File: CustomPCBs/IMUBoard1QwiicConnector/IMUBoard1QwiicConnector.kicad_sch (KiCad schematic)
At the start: 14 parts, among them J1 Conn_01x04_Pin, Y1 32.768kHz

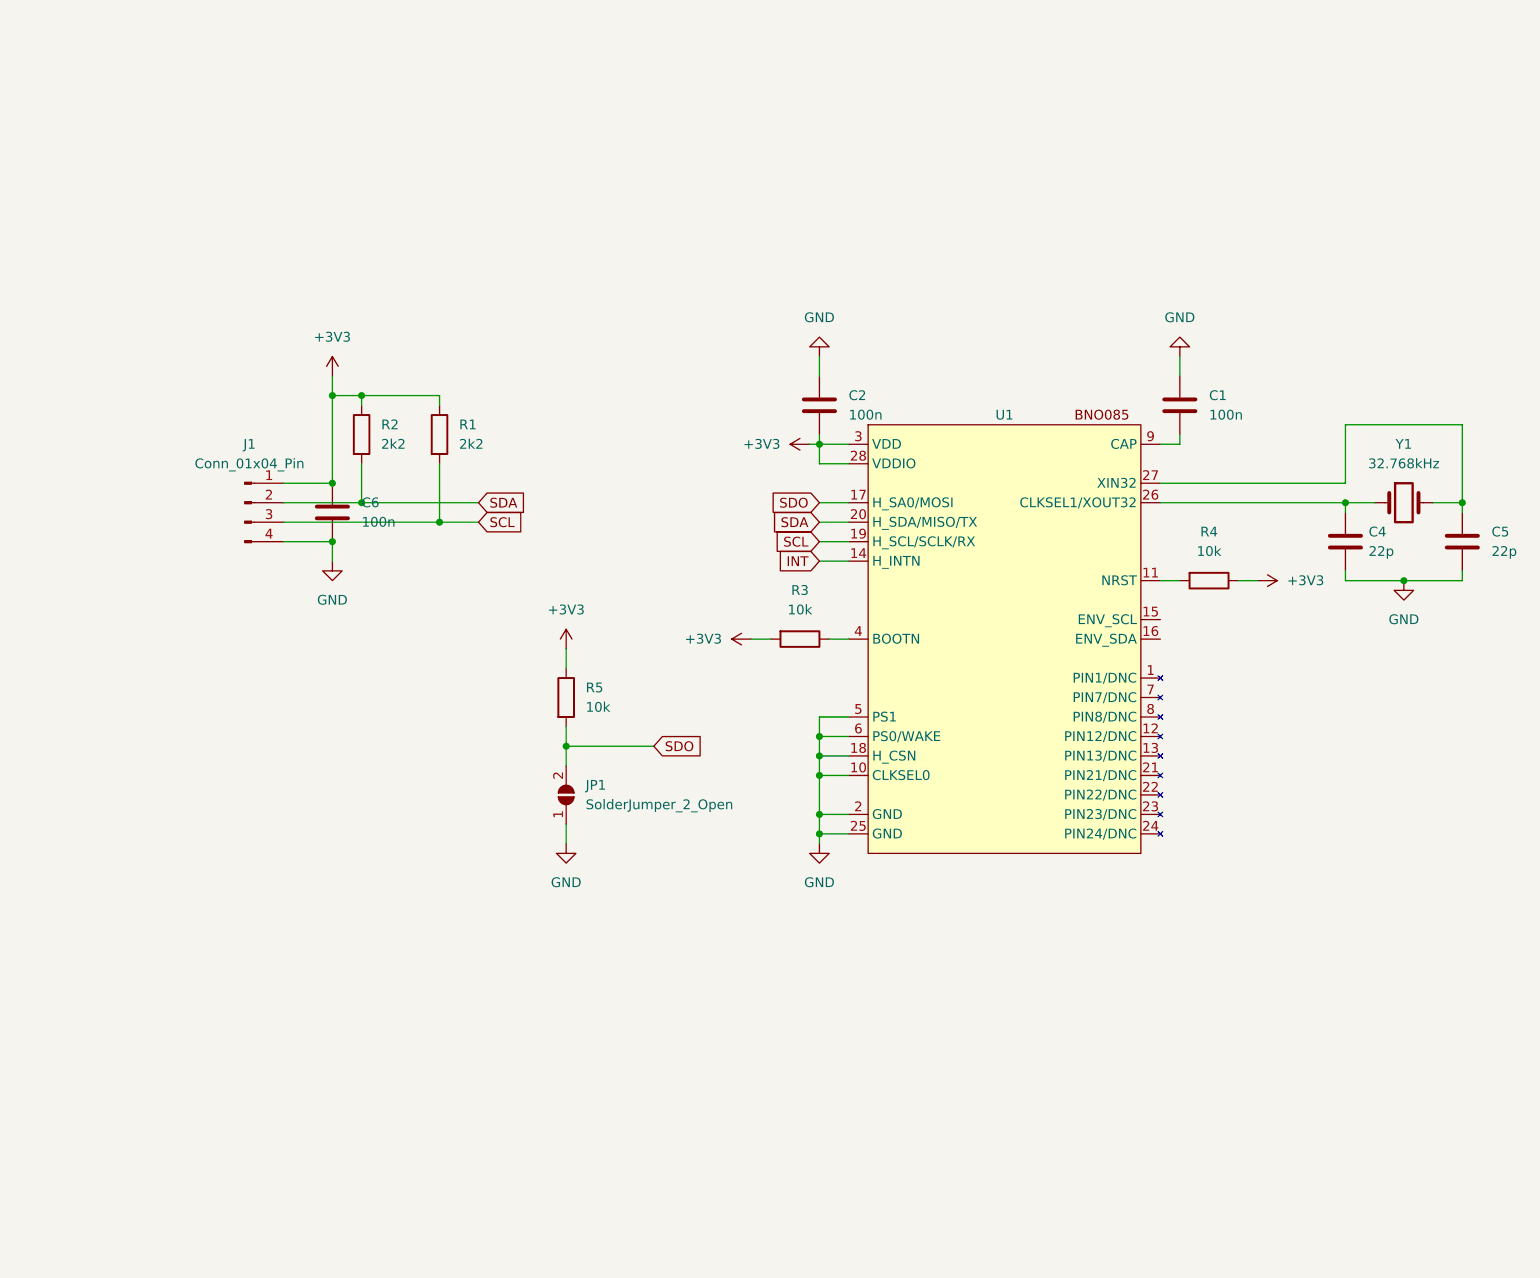
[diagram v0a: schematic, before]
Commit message: Updating smallest IMU board
Will probably make it even smaller by hardwiring PS0, PS1 and SDO pins.
And maybe even the connector can go to give room for a cable bundle of 4
wires soldered to the board directly.
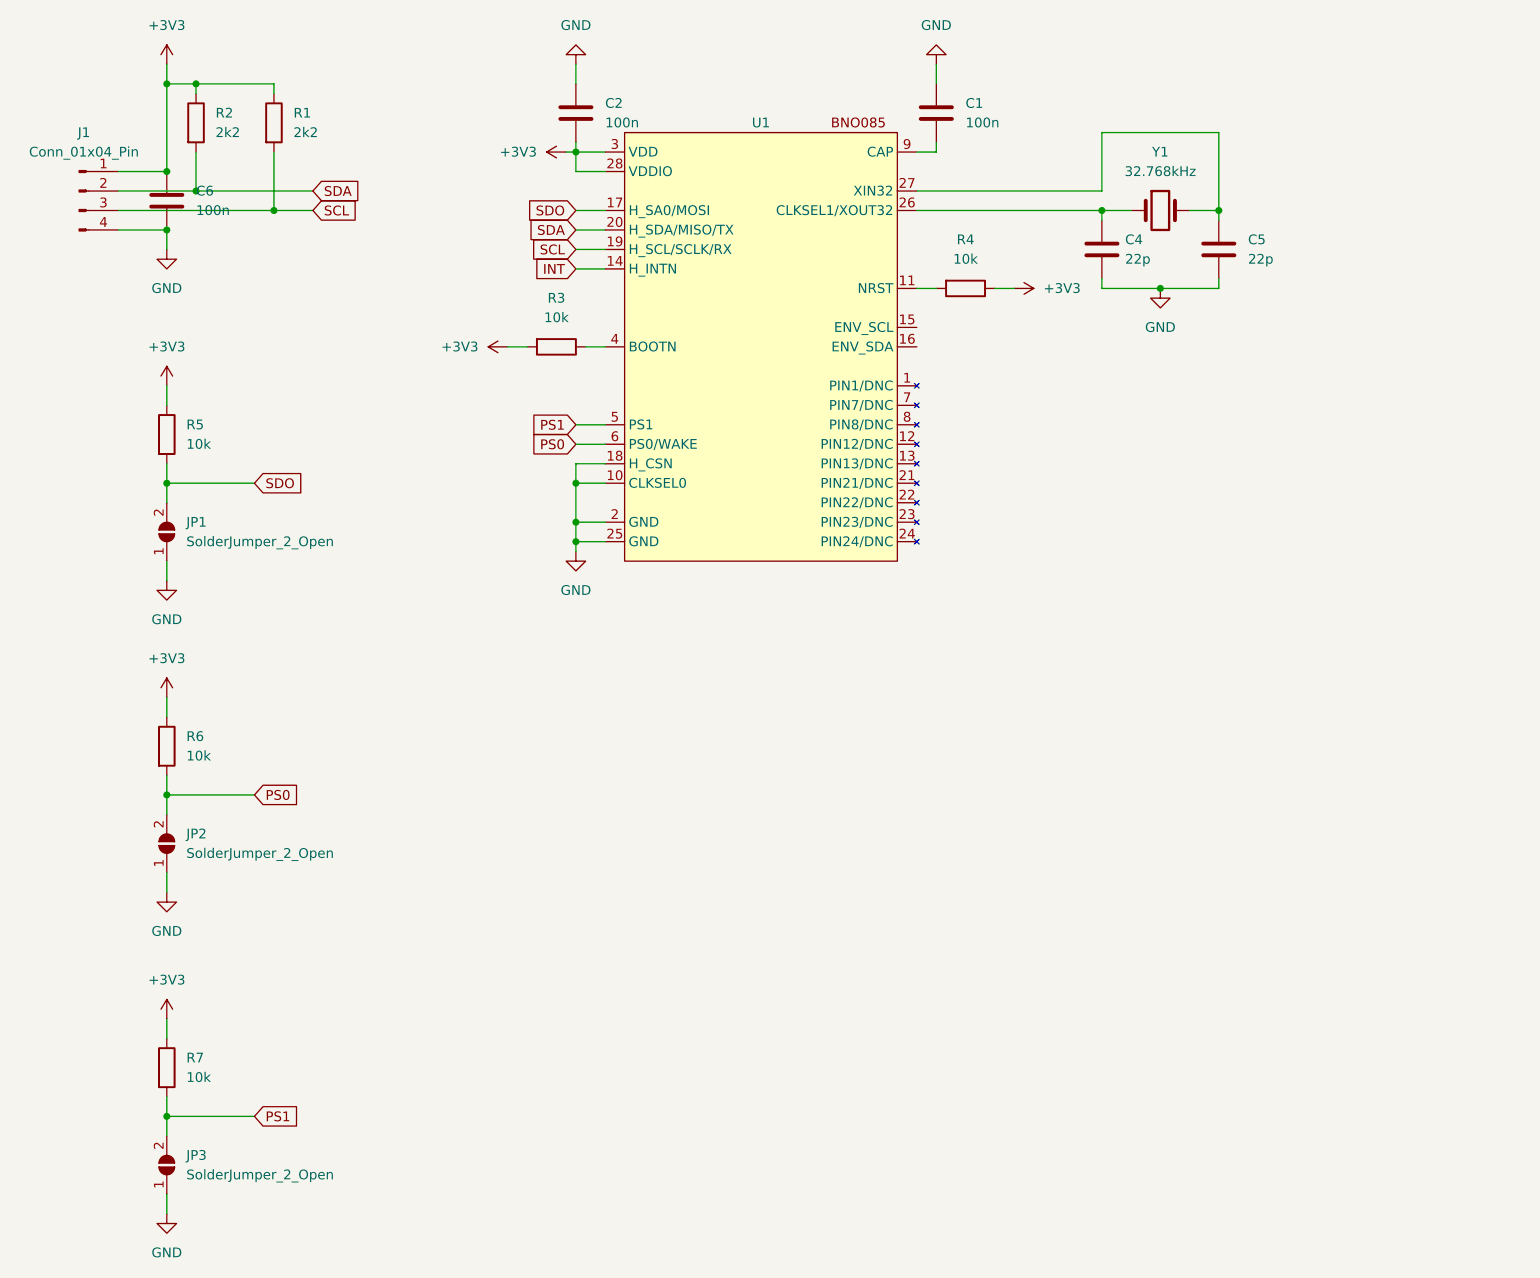
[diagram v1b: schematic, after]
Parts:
- added JP2, JP3: SolderJumper_2_Open, Jumper:SolderJumper-2_P1.3mm_Open_Pad1.0x1.5mm, symbol Jumper:SolderJumper_2_Open
- added R6, R7: 10k, Resistor_SMD:R_0603_1608Metric, symbol Device:R
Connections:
- net +3V3: now also R6.1, R7.1
- net GND: now also JP2.1 (A), JP3.1 (A); no longer U1.5 (PS1), U1.6 (PS0/WAKE)
- new net PS0: JP2.2 (B), R6.2, U1.6 (PS0/WAKE)
- new net PS1: JP3.2 (B), R7.2, U1.5 (PS1)
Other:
- moved on the sheet: C1, C2, C4, C5, C6, J1, JP1, R1, R2, R3, R4, R5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

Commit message: Making the IMU board on the finger tip smaller
Just saving work to continue at lunch, will use 4 layer pcb for the
board to be as small as possible
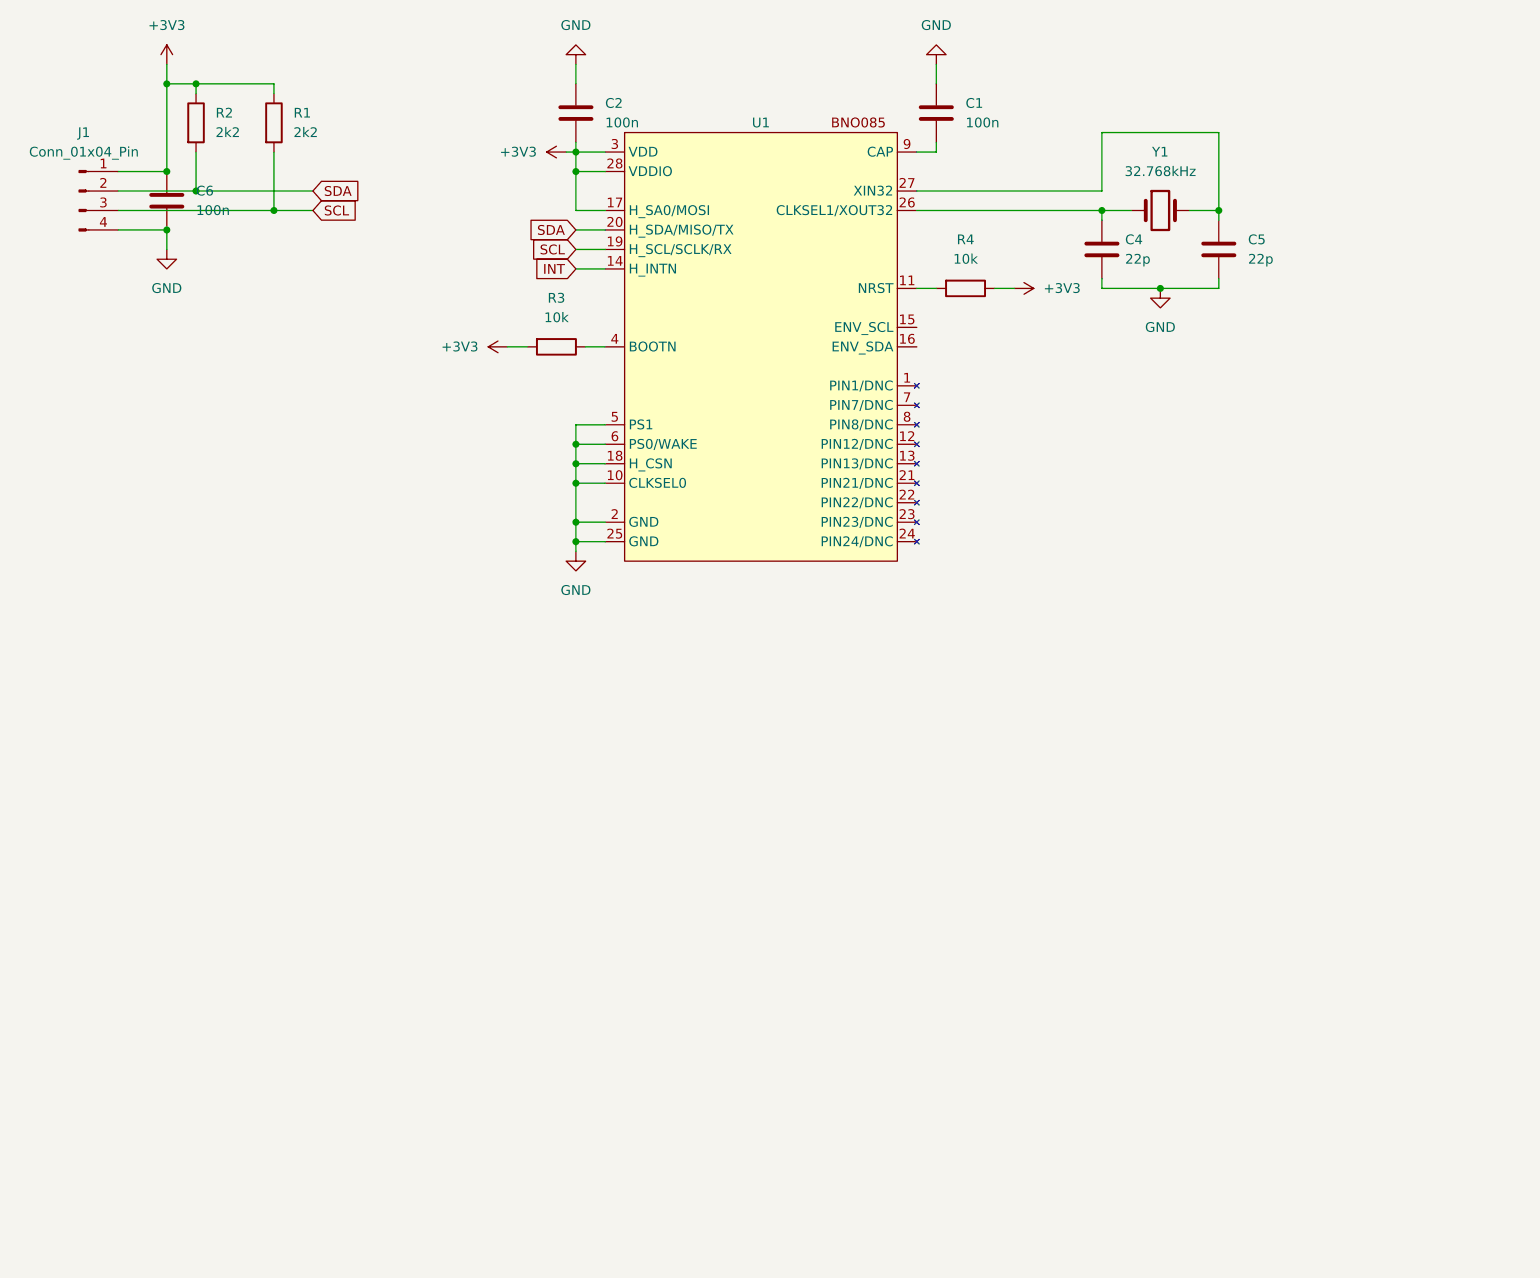
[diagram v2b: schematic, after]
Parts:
- removed JP1, JP2, JP3: SolderJumper_2_Open, Jumper:SolderJumper-2_P1.3mm_Open_Pad1.0x1.5mm, symbol Jumper:SolderJumper_2_Open
- removed R5, R6, R7: 10k, Resistor_SMD:R_0603_1608Metric, symbol Device:R
- C1, C2, C4, C5, C6: footprint Capacitor_SMD:C_0603_1608Metric -> Capacitor_SMD:C_0402_1005Metric
- R1, R2, R3, R4: footprint Resistor_SMD:R_0603_1608Metric -> Resistor_SMD:R_0402_1005Metric
- Y1: footprint Crystal:Crystal_SMD_3215-2Pin_3.2x1.5mm -> Crystal:Crystal_SMD_2012-2Pin_2.0x1.2mm
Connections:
- net PS0 is gone; now on net GND: U1.6 (PS0/WAKE)
- net PS1 is gone; now on net GND: U1.5 (PS1)
- net SDO is gone; now on net +3V3: U1.17 (H_SA0/MOSI)
